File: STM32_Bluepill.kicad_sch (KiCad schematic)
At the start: 13 parts

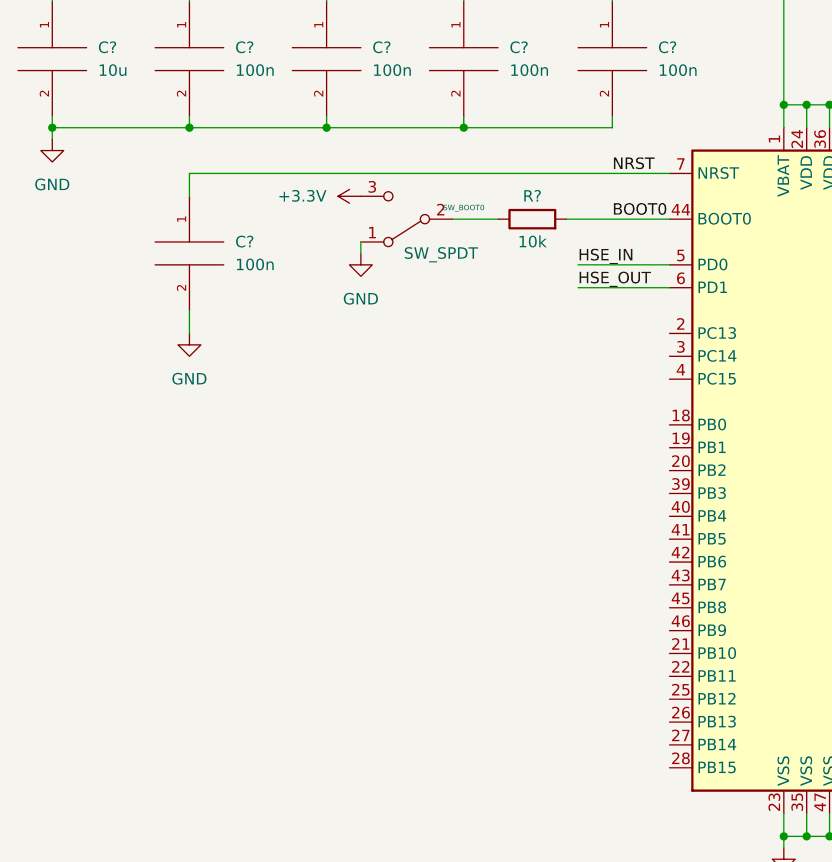
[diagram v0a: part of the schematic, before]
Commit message: Schematic: Add crystal circuitry
	- STM has a crystal design guide - Application Note # AN2867
	- 10 pF crystal with a stray capacitance of 3-5 pF gives us
	  around 5pF, multiplying by 2 gives 10pF caps attached to the
	  crystal
		- Calculating these caps also found in the datasheet
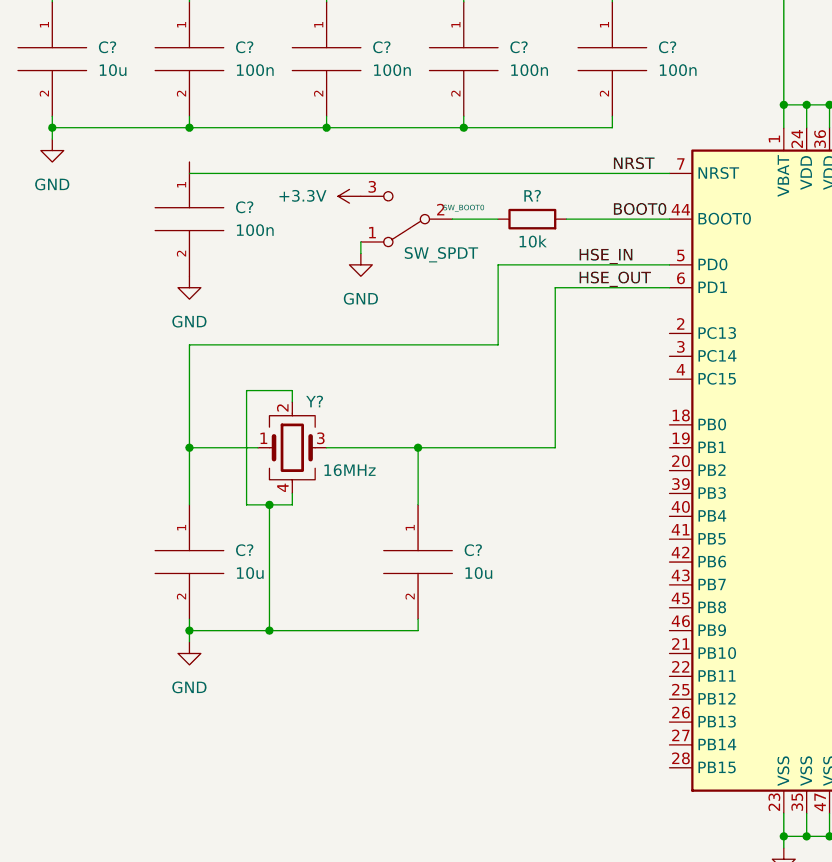
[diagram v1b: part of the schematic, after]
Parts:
- added C? (x2): 10u, symbol pspice:C
- added Y?: 16MHz, symbol Device:Crystal_GND24
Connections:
- net GND: now also C?.2, C?.2, Y?.2, Y?.4
- net HSE_IN: now also C?.1, Y?.1
- net HSE_OUT: now also C?.1, Y?.3
- net NRST: no longer C?.1
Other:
- moved on the sheet: C?

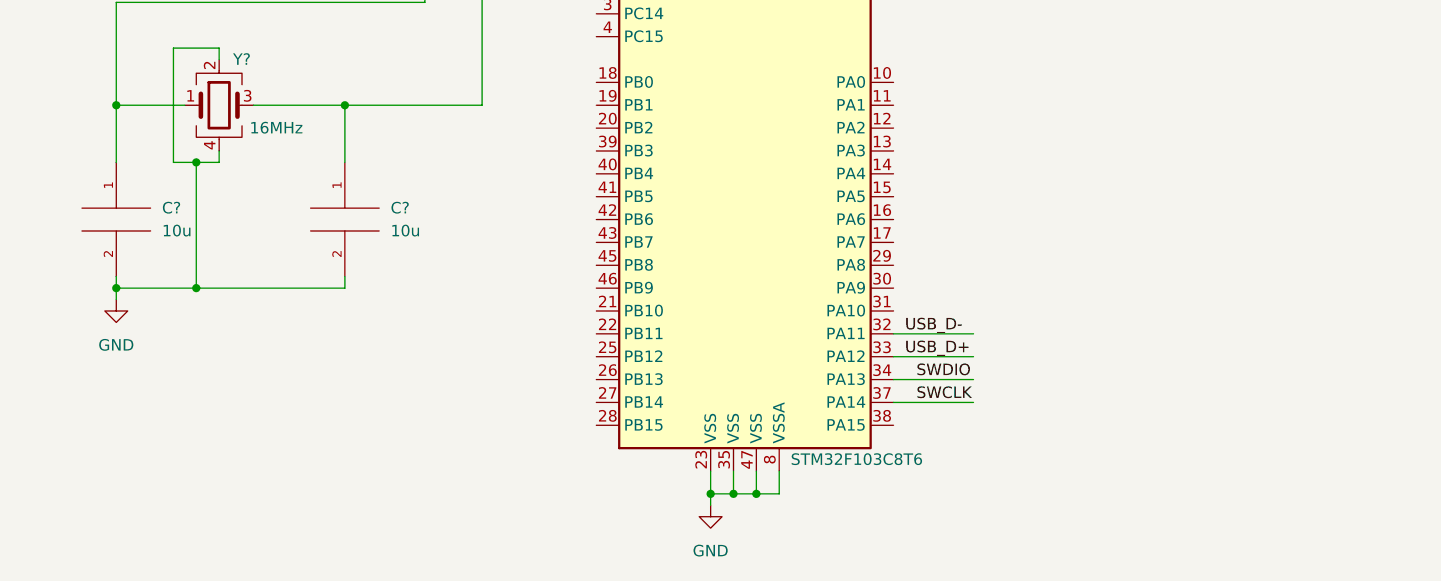
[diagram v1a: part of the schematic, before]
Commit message: Schematic: Add USB B Micro and STM USB app note
	- Use USB App note from STM to get what pullup resistor value to
	  use on the USB_D+ line
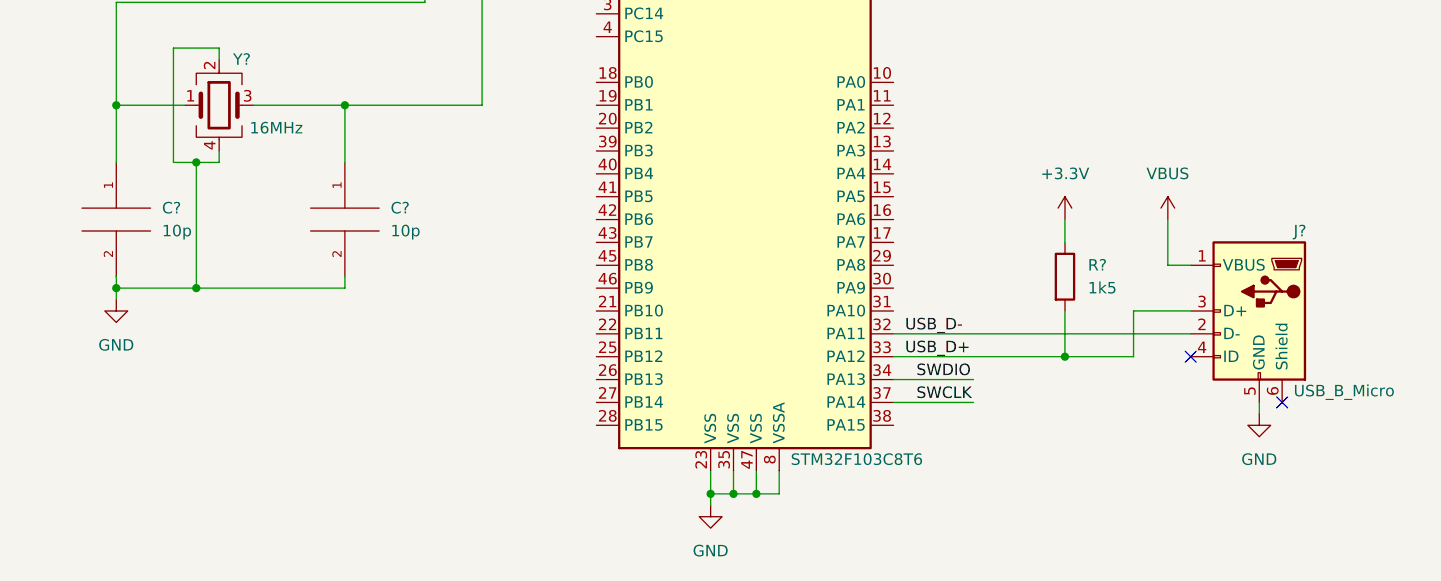
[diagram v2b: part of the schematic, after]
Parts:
- added J?: USB_B_Micro, symbol Connector:USB_B_Micro
- added R?: 1k5, symbol Device:R
- C? (x2): value 10u -> 10p
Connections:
- net +3.3V: now also R?.1
- net GND: now also J?.5 (GND)
- net USB_D+: now also J?.3 (D+), R?.2
- net USB_D-: now also J?.2 (D-)
- new net VBUS: J?.1 (VBUS)
- no-connect marks 0 -> 2
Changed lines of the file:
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@@
   (junction (at 49.53 105.41) (diameter 0) (color 0 0 0 0)
   )
+  (junction (at 154.94 113.03) (diameter 0) (color 0 0 0 0)
+  )
   (junction (at 143.51 34.29) (diameter 0) (color 0 0 0 0)
   )
@@
   (junction (at 171.45 34.29) (diameter 0) (color 0 0 0 0)
   )
+  (no_connect (at 179.07 118.11))
+  (no_connect (at 168.91 113.03))
   (wire (pts (xy 179.07 34.29) (xy 184.15 34.29))
     (stroke (width 0) (type default) (color 0 0 0 0))
@@
     (stroke (width 0) (type default) (color 0 0 0 0))
   )
+  (wire (pts (xy 154.94 97.79) (xy 154.94 100.33))
+    (stroke (width 0) (type default) (color 0 0 0 0))
+  )
   (wire (pts (xy 115.57 33.02) (xy 115.57 34.29))
     (stroke (width 0) (type default) (color 0 0 0 0))
@@
     (stroke (width 0) (type default) (color 0 0 0 0))
   )
+  (wire (pts (xy 168.91 107.95) (xy 162.56 107.95))
+    (stroke (width 0) (type default) (color 0 0 0 0))
+  )
   (wire (pts (xy 74.93 105.41) (xy 74.93 104.14))
     (stroke (width 0) (type default) (color 0 0 0 0))
@@
     (stroke (width 0) (type default) (color 0 0 0 0))
   )
+  (wire (pts (xy 154.94 113.03) (xy 162.56 113.03))
+    (stroke (width 0) (type default) (color 0 0 0 0))
+  )
+  (wire (pts (xy 166.37 102.87) (xy 168.91 102.87))
+    (stroke (width 0) (type default) (color 0 0 0 0))
+  )
   (wire (pts (xy 102.87 54.61) (xy 49.53 54.61))
     (stroke (width 0) (type default) (color 0 0 0 0))
@@
     (stroke (width 0) (type default) (color 0 0 0 0))
   )
-  (wire (pts (xy 135.89 113.03) (xy 144.78 113.03))
+  (wire (pts (xy 135.89 113.03) (xy 154.94 113.03))
     (stroke (width 0) (type default) (color 0 0 0 0))
   )
@@
     (stroke (width 0) (type default) (color 0 0 0 0))
   )
-  (wire (pts (xy 135.89 110.49) (xy 144.78 110.49))
+  (wire (pts (xy 135.89 110.49) (xy 168.91 110.49))
     (stroke (width 0) (type default) (color 0 0 0 0))
   )
@@
     (stroke (width 0) (type default) (color 0 0 0 0))
   )
+  (wire (pts (xy 166.37 97.79) (xy 166.37 102.87))
+    (stroke (width 0) (type default) (color 0 0 0 0))
+  )
   (wire (pts (xy 118.11 128.27) (xy 120.65 128.27))
     (stroke (width 0) (type default) (color 0 0 0 0))
@@
     (stroke (width 0) (type default) (color 0 0 0 0))
   )
+  (wire (pts (xy 176.53 118.11) (xy 176.53 119.38))
+    (stroke (width 0) (type default) (color 0 0 0 0))
+  )
   (wire (pts (xy 184.15 33.02) (xy 184.15 34.29))
     (stroke (width 0) (type default) (color 0 0 0 0))
@@
     (stroke (width 0) (type default) (color 0 0 0 0))
   )
+  (wire (pts (xy 154.94 107.95) (xy 154.94 113.03))
+    (stroke (width 0) (type default) (color 0 0 0 0))
+  )
   (wire (pts (xy 120.65 46.99) (xy 123.19 46.99))
     (stroke (width 0) (type default) (color 0 0 0 0))
@@
   )
   (wire (pts (xy 49.53 105.41) (xy 49.53 106.68))
+    (stroke (width 0) (type default) (color 0 0 0 0))
+  )
+  (wire (pts (xy 162.56 107.95) (xy 162.56 113.03))
     (stroke (width 0) (type default) (color 0 0 0 0))
   )
@@
     )
     (property "Datasheet" "" (id 3) (at 125.73 33.02 0)
+      (effects (font (size 1.27 1.27)) hide)
+    )
+    (pin "1")
+  )
+  (symbol (lib_id "power:GND") (at 176.53 119.38 0) (unit 1)
+    (in_bom yes) (on_board yes) (fields_autoplaced)
+    (property "Reference" "#PWR?" (id 0) (at 176.53 125.73 0)
+      (effects (font (size 1.27 1.27)) hide)
+    )
+    (property "Value" "GND" (id 1) (at 176.53 124.46 0))
+    (property "Footprint" "" (id 2) (at 176.53 119.38 0)
+      (effects (font (size 1.27 1.27)) hide)
+    )
+    (property "Datasheet" "" (id 3) (at 176.53 119.38 0)
       (effects (font (size 1.27 1.27)) hide)
     )
@@
     (pin "1")
   )
+  (symbol (lib_id "Device:R") (at 154.94 104.14 0) (unit 1)
+    (in_bom yes) (on_board yes) (fields_autoplaced)
+    (property "Reference" "R?" (id 0) (at 157.48 102.8699 0)
+      (effects (font (size 1.27 1.27)) (justify left))
+    )
+    (property "Value" "1k5" (id 1) (at 157.48 105.4099 0)
+      (effects (font (size 1.27 1.27)) (justify left))
+    )
+    (property "Footprint" "" (id 2) (at 153.162 104.14 90)
+      (effects (font (size 1.27 1.27)) hide)
+    )
+    (property "Datasheet" "~" (id 3) (at 154.94 104.14 0)
+      (effects (font (size 1.27 1.27)) hide)
+    )
+    (pin "1")
+    (pin "2")
+  )
   (symbol (lib_id "pspice:C") (at 49.53 59.69 0) (unit 1)
     (in_bom yes) (on_board yes) (fields_autoplaced)
@@
       (effects (font (size 1.27 1.27)) (justify left))
     )
-    (property "Value" "10u" (id 1) (at 80.01 99.0599 0)
+    (property "Value" "10p" (id 1) (at 80.01 99.0599 0)
       (effects (font (size 1.27 1.27)) (justify left))
     )
@@
     (pin "2")
   )
+  (symbol (lib_id "Connector:USB_B_Micro") (at 176.53 107.95 0) (mirror y) (unit 1)
+    (in_bom yes) (on_board yes)
+    (property "Reference" "J?" (id 0) (at 180.34 99.06 0)
+      (effects (font (size 1.27 1.27)) (justify right))
+    )
+    (property "Value" "USB_B_Micro" (id 1) (at 180.34 116.84 0)
+      (effects (font (size 1.27 1.27)) (justify right))
+    )
+    (property "Footprint" "" (id 2) (at 172.72 109.22 0)
+      (effects (font (size 1.27 1.27)) hide)
+    )
+    (property "Datasheet" "~" (id 3) (at 172.72 109.22 0)
+      (effects (font (size 1.27 1.27)) hide)
+    )
+    (pin "1")
+    (pin "2")
+    (pin "3")
+    (pin "4")
+    (pin "5")
+    (pin "6")
+  )
   (symbol (lib_id "pspice:C") (at 49.53 41.91 0) (unit 1)
     (in_bom yes) (on_board yes) (fields_autoplaced)
@@
     (pin "1")
     (pin "2")
+  )
+  (symbol (lib_id "power:VBUS") (at 166.37 97.79 0) (unit 1)
+    (in_bom yes) (on_board yes) (fields_autoplaced)
+    (property "Reference" "#PWR?" (id 0) (at 166.37 101.6 0)
+      (effects (font (size 1.27 1.27)) hide)
+    )
+    (property "Value" "VBUS" (id 1) (at 166.37 92.71 0))
+    (property "Footprint" "" (id 2) (at 166.37 97.79 0)
+      (effects (font (size 1.27 1.27)) hide)
+    )
+    (property "Datasheet" "" (id 3) (at 166.37 97.79 0)
+      (effects (font (size 1.27 1.27)) hide)
+    )
+    (pin "1")
+  )
+  (symbol (lib_id "power:+3.3V") (at 154.94 97.79 0) (unit 1)
+    (in_bom yes) (on_board yes) (fields_autoplaced)
+    (property "Reference" "#PWR?" (id 0) (at 154.94 101.6 0)
+      (effects (font (size 1.27 1.27)) hide)
+    )
+    (property "Value" "+3.3V" (id 1) (at 154.94 92.71 0))
+    (property "Footprint" "" (id 2) (at 154.94 97.79 0)
+      (effects (font (size 1.27 1.27)) hide)
+    )
+    (property "Datasheet" "" (id 3) (at 154.94 97.79 0)
+      (effects (font (size 1.27 1.27)) hide)
+    )
+    (pin "1")
   )
   (symbol (lib_id "power:GND") (at 184.15 50.8 0) (unit 1)
@@
       (effects (font (size 1.27 1.27)) (justify left))
     )
-    (property "Value" "10u" (id 1) (at 54.61 99.0599 0)
+    (property "Value" "10p" (id 1) (at 54.61 99.0599 0)
       (effects (font (size 1.27 1.27)) (justify left))
     )
@@
       (reference "#PWR?") (unit 1) (value "+3.3VA") (footprint "")
     )
+    (path "/2ea86650-3661-4612-a88f-c12ec56c8271"
+      (reference "#PWR?") (unit 1) (value "GND") (footprint "")
+    )
     (path "/41f4187e-61d8-407d-b7b8-d2d0ad0cd785"
       (reference "#PWR?") (unit 1) (value "GND") (footprint "")
@@
       (reference "#PWR?") (unit 1) (value "GND") (footprint "")
     )
+    (path "/b62cedec-1117-4b50-ba96-c7a34f9bd261"
+      (reference "#PWR?") (unit 1) (value "VBUS") (footprint "")
+    )
+    (path "/b8f352fa-7eee-4eed-aa13-4840aa038ddf"
+      (reference "#PWR?") (unit 1) (value "+3.3V") (footprint "")
+    )
     (path "/bec7b0b5-43f0-4ea5-9c6c-28a0224569cb"
       (reference "#PWR?") (unit 1) (value "GND") (footprint "")
@@
     )
     (path "/9a2eb0b3-89cd-4e1a-9a4f-22dd779e9c77"
-      (reference "C?") (unit 1) (value "10u") (footprint "")
+      (reference "C?") (unit 1) (value "10p") (footprint "")
     )
     (path "/a4740f12-08c6-4aec-b367-d8c2d48bb45d"
@@
     )
     (path "/c4c69945-b556-44b7-8279-6a88b68a2724"
-      (reference "C?") (unit 1) (value "10u") (footprint "")
+      (reference "C?") (unit 1) (value "10p") (footprint "")
     )
     (path "/f3d3ae94-820c-4258-bc6b-8c8dd19c3469"
@@
       (reference "FB?") (unit 1) (value "120R") (footprint "")
     )
+    (path "/9f1c510e-32d3-4302-89a0-0925ff949f4e"
+      (reference "J?") (unit 1) (value "USB_B_Micro") (footprint "")
+    )
     (path "/415aa6bb-21e9-4dd6-a1b4-c89c0b826bee"
       (reference "R?") (unit 1) (value "10k") (footprint "")
     )
+    (path "/878c06a9-9fe0-4d98-8ca9-29ee5cfd6924"
+      (reference "R?") (unit 1) (value "1k5") (footprint "")
+    )
     (path "/d5578dea-06c9-4c48-a263-f56a9b1bb322"
